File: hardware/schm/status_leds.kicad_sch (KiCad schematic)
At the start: 13 parts, among them J2 Orange TinySLED, Q1 AO3402, U10 SK9822-EC20, U8 SN74AHCT1G125, U9 SN74AHCT1G125

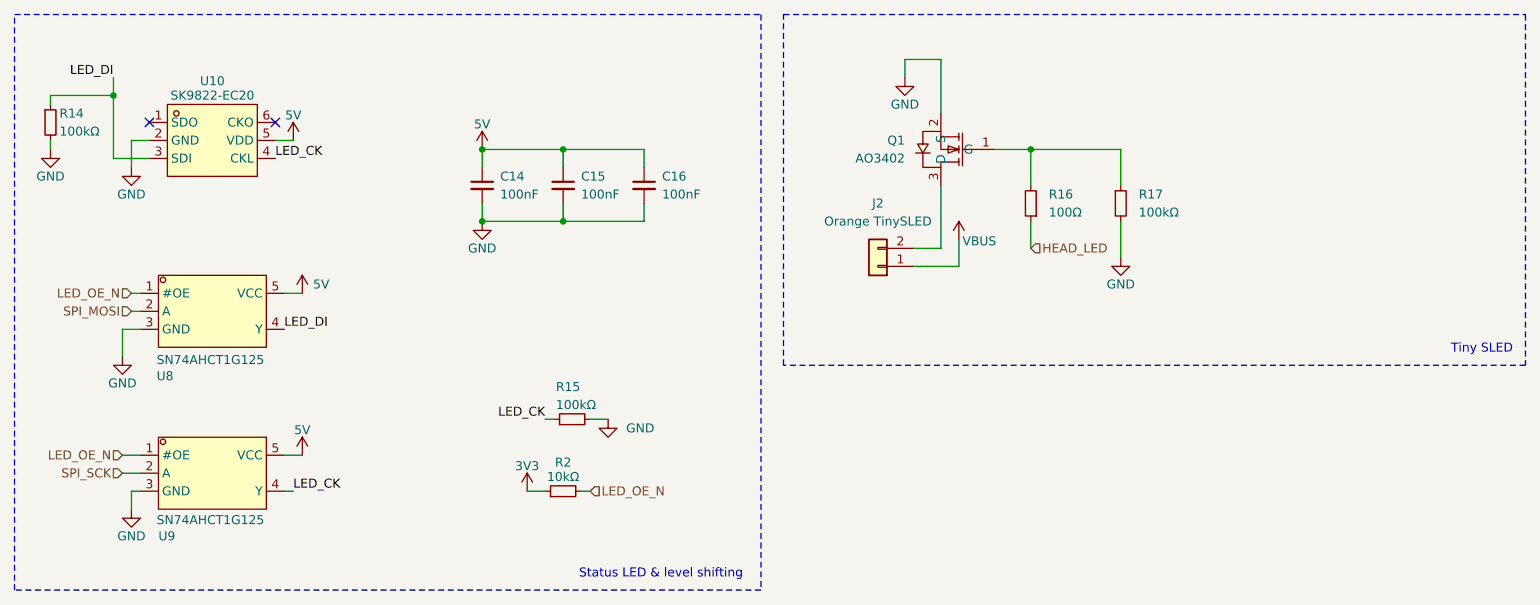
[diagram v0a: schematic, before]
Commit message: feat: first bit of routing and double leds + fixes
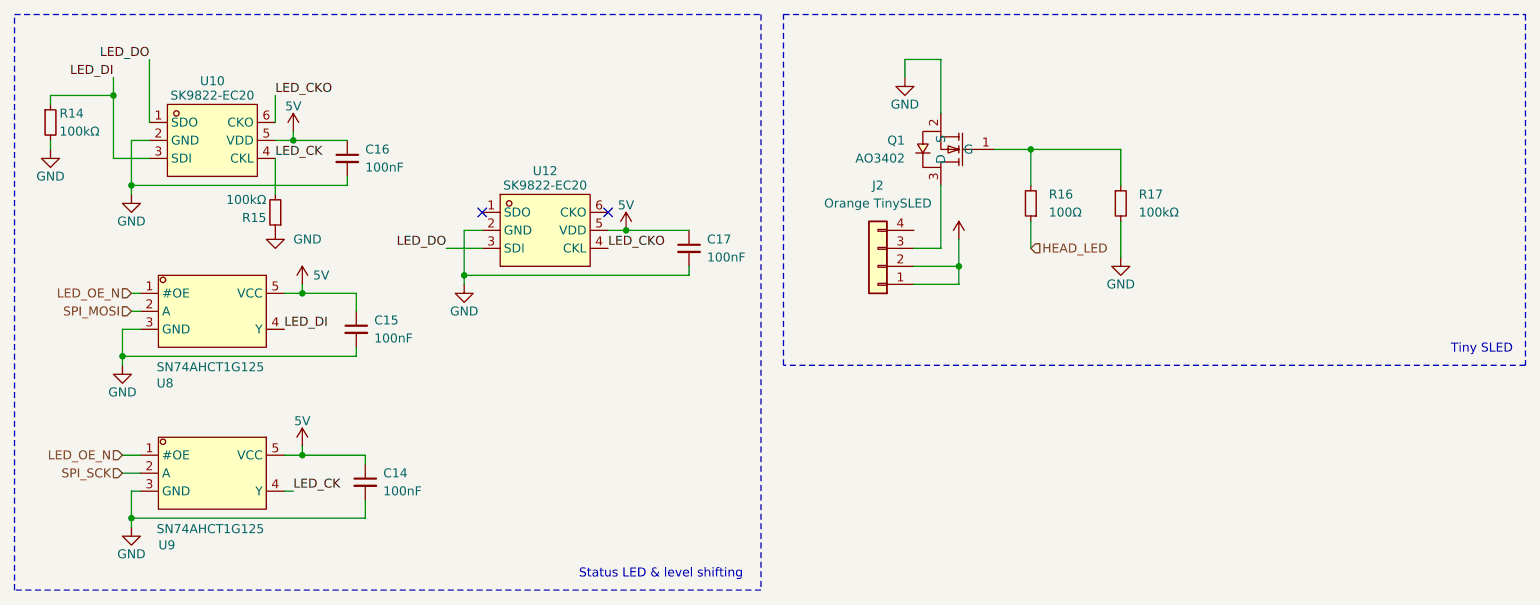
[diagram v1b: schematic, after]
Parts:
- removed R2: 10kΩ, Resistor_SMD:R_0402_1005Metric, symbol Device:R_Small
- added C17: 100nF, Capacitor_SMD:C_0402_1005Metric, symbol Device:C_Small
- added U12: SK9822-EC20, Library:LED-SMD_6P-L2.0-W2.0-P0.80-TL, symbol Library:SK9822-EC20
- J2: footprint Connector_Wire:SolderWire-0.25sqmm_1x02_P4.2mm_D0.65mm_OD1.7mm_Relief -> Connector_Wire:SolderWire-0.25sqmm_1x04_P4.2mm_D0.65mm_OD1.7mm; symbol Connector_Generic:Conn_01x02 -> Connector_Generic:Conn_01x04
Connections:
- net 5V: now also C17.1, U12.5 (VDD)
- net GND: now also R15.1, C17.2, U12.2 (GND); no longer R15.2
- net LED_CK: now also R15.2; no longer R15.1
- net VBUS: now also J2.2 (Pin_2)
- net at Q1.3 (D): now also J2.3 (Pin_3); no longer J2.2 (Pin_2)
- net LED_DO: now reaches U10.1 (SDO)
- net LED_DO: now also U12.3 (SDI)
- net LED_CKO: now reaches U10.6 (CKO)
- net LED_CKO: now also U12.4 (CKL)

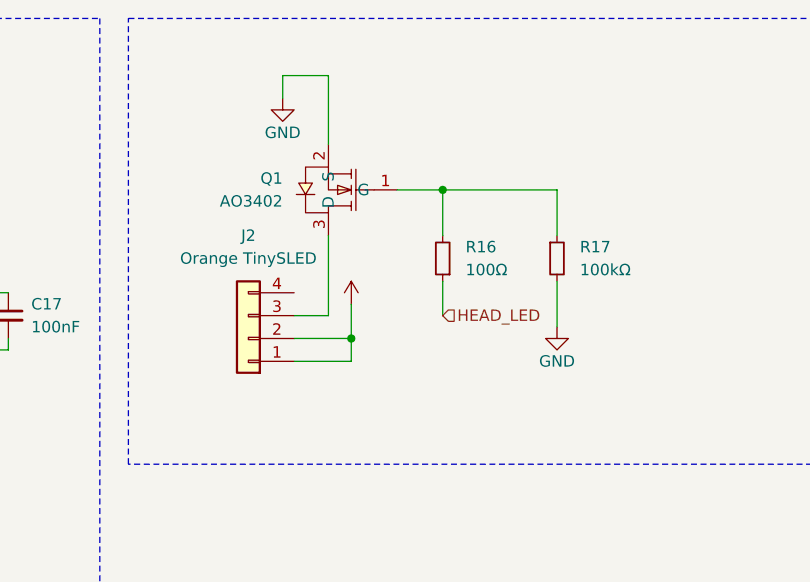
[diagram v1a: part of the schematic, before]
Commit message: feat: 4 layer route
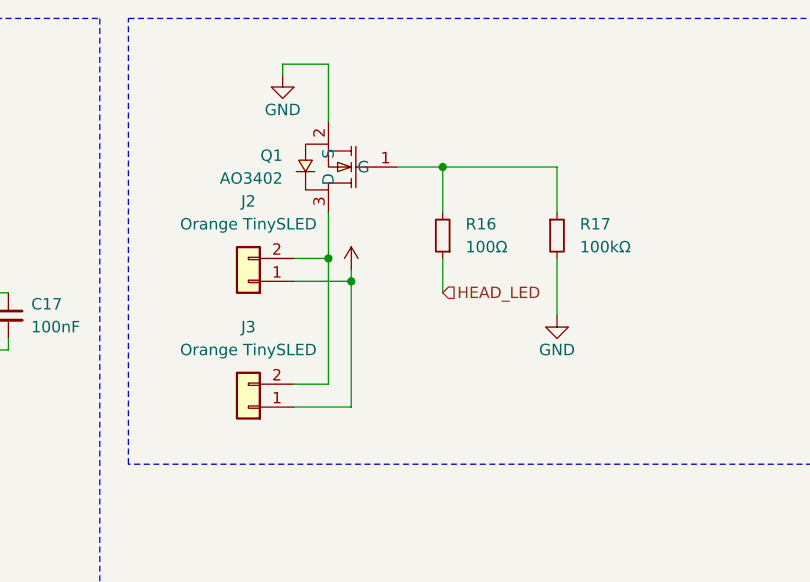
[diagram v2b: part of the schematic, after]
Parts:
- added J3: Orange TinySLED, Connector_Wire:SolderWire-0.25sqmm_1x02_P4.2mm_D0.65mm_OD1.7mm, symbol Connector_Generic:Conn_01x02
- J2: footprint Connector_Wire:SolderWire-0.25sqmm_1x04_P4.2mm_D0.65mm_OD1.7mm -> Connector_Wire:SolderWire-0.25sqmm_1x02_P4.2mm_D0.65mm_OD1.7mm; symbol Connector_Generic:Conn_01x04 -> Connector_Generic:Conn_01x02
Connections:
- net VBUS: now also J3.1 (Pin_1); no longer J2.2 (Pin_2)
- net at Q1.3 (D): now also J2.2 (Pin_2), J3.2 (Pin_2); no longer J2.3 (Pin_3)
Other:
- moved on the sheet: Q1, R16, R17

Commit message: feat: add bom placement
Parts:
- C14, C15, C16, C17: LCSC Part NONE -> C169834
- J2, J3: now left out of the parts list
- R14, R15, R17: LCSC Part NONE -> C2077080
- R16: LCSC Part NONE -> C1884631
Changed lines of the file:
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@@
 		(body_style 1)
 		(exclude_from_sim no)
-		(in_bom yes)
-		(on_board yes)
-		(in_pos_files yes)
+		(in_bom no)
+		(on_board yes)
+		(in_pos_files no)
 		(dnp no)
 		(fields_autoplaced yes)
@@
 			)
 		)
-		(property "LCSC Part" "NONE"
+		(property "LCSC Part" "C2077080"
 			(at 113.51 -235.9 0)
 			(hide yes)
@@
 			)
 		)
-		(property "LCSC Part" "NONE"
+		(property "LCSC Part" "C169834"
 			(at -231.14 -153.67 0)
 			(hide yes)
@@
 			)
 		)
-		(property "LCSC Part" "NONE"
+		(property "LCSC Part" "C169834"
 			(at -269.24 -142.24 0)
 			(hide yes)
@@
 			)
 		)
-		(property "LCSC Part" "NONE"
+		(property "LCSC Part" "C2077080"
 			(at 339.09 275.59 0)
 			(hide yes)
@@
 			)
 		)
-		(property "LCSC Part" "NONE"
+		(property "LCSC Part" "C2077080"
 			(at -266.7 -184.15 0)
 			(hide yes)
@@
 			)
 		)
-		(property "LCSC Part" "NONE"
+		(property "LCSC Part" "C169834"
 			(at -259.08 -120.65 0)
 			(hide yes)
@@
 			)
 		)
-		(property "LCSC Part" "NONE"
+		(property "LCSC Part" "C169834"
 			(at -279.4 -166.37 0)
 			(hide yes)
@@
 			)
 		)
-		(property "LCSC Part" "NONE"
+		(property "LCSC Part" "C1884631"
 			(at 201.69 314.64 0)
 			(hide yes)
@@
 		(body_style 1)
 		(exclude_from_sim no)
-		(in_bom yes)
-		(on_board yes)
-		(in_pos_files yes)
+		(in_bom no)
+		(on_board yes)
+		(in_pos_files no)
 		(dnp no)
 		(fields_autoplaced yes)
